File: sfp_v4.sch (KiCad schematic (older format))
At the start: 75 parts, among them J102 SMA, J104 SMA, J106 SMA, P101 SFP-CONNECTOR, P103 CONN_01X01, P106 CONN_01X01, T101 ADT2-1T, T102 ADT2-1T, U101 LMH6702, U102 LMH6702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

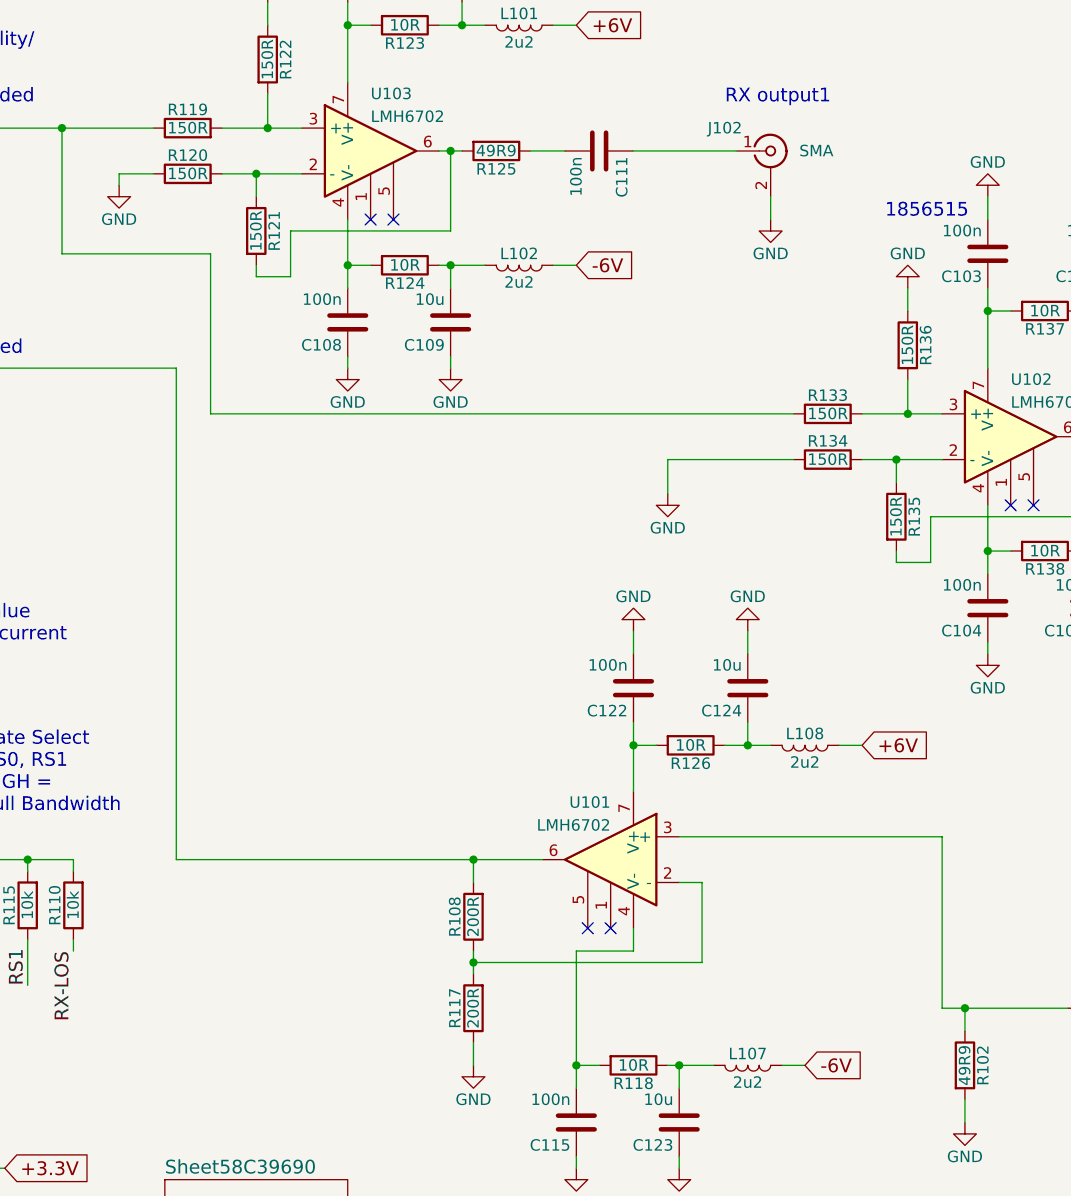
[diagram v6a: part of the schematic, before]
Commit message: bump gain to 1+240/60
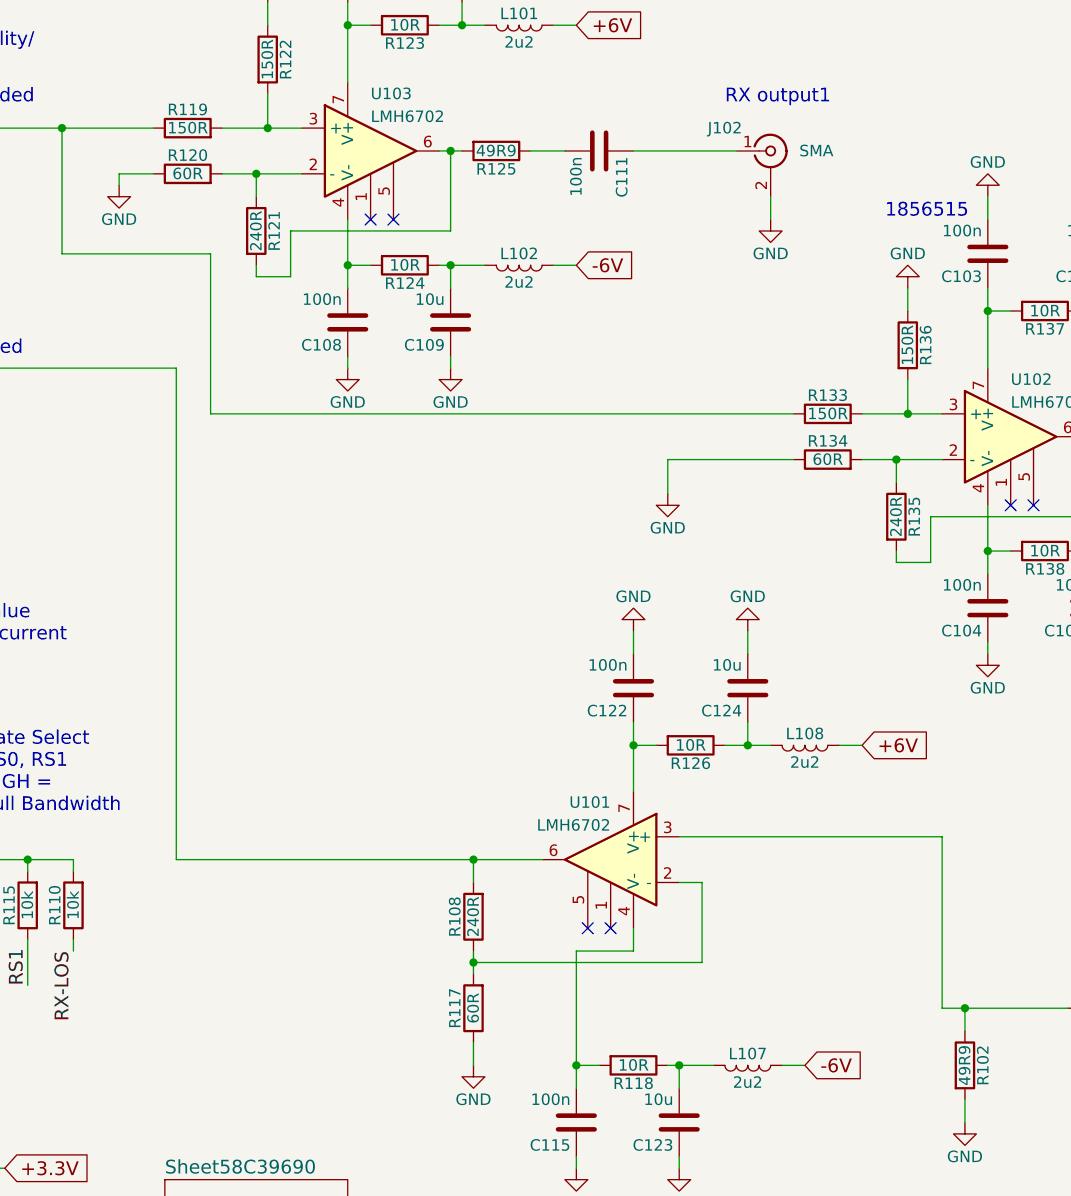
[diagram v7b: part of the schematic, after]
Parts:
- R108: value 200R -> 240R
- R117: value 200R -> 60R
- R120, R134: value 150R -> 60R
- R121, R135: value 150R -> 240R
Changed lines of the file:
@@
 P 5050 1900
 F 0 "R120" V 5130 1900 50  0000 C CNN
-F 1 "150R" V 5050 1900 50  0000 C CNN
+F 1 "60R" V 5050 1900 50  0000 C CNN
 F 2 "Resistors_SMD:R_0805" V 4980 1900 30  0001 C CNN
 F 3 "" H 5050 1900 30  0000 C CNN
@@
 P 5350 2150
 F 0 "R121" V 5430 2150 50  0000 C CNN
-F 1 "150R" V 5350 2150 50  0000 C CNN
+F 1 "240R" V 5350 2150 50  0000 C CNN
 F 2 "Resistors_SMD:R_0805" V 5280 2150 30  0001 C CNN
 F 3 "" H 5350 2150 30  0000 C CNN
@@
 P 8150 3400
 F 0 "R135" V 8230 3400 50  0000 C CNN
-F 1 "150R" V 8150 3400 50  0000 C CNN
+F 1 "240R" V 8150 3400 50  0000 C CNN
 F 2 "Resistors_SMD:R_0805" V 8080 3400 30  0001 C CNN
 F 3 "" H 8150 3400 30  0000 C CNN
@@
 P 7850 3150
 F 0 "R134" V 7930 3150 50  0000 C CNN
-F 1 "150R" V 7850 3150 50  0000 C CNN
+F 1 "60R" V 7850 3150 50  0000 C CNN
 F 2 "Resistors_SMD:R_0805" V 7780 3150 30  0001 C CNN
 F 3 "" H 7850 3150 30  0000 C CNN
@@
 P 6300 5150
 F 0 "R108" V 6380 5150 50  0000 C CNN
-F 1 "200R" V 6300 5150 50  0000 C CNN
+F 1 "240R" V 6300 5150 50  0000 C CNN
 F 2 "Resistors_SMD:R_0805" V 6230 5150 50  0001 C CNN
 F 3 "" H 6300 5150 50  0001 C CNN
@@
 P 6300 5550
 F 0 "R117" V 6380 5550 50  0000 C CNN
-F 1 "200R" V 6300 5550 50  0000 C CNN
+F 1 "60R" V 6300 5550 50  0000 C CNN
 F 2 "Resistors_SMD:R_0805" V 6230 5550 50  0001 C CNN
 F 3 "" H 6300 5550 50  0001 C CNN

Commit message: tune component values
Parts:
- R108: value 240R -> 200R
- R117: value 60R -> 200R
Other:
- note removed: "BNC: 1076295"
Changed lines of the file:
@@
 Text Notes 3250 7200 0    60   ~ 0
 1u Inductor\n445-6756-1-ND
-Text Notes 10300 5050 0    60   ~ 0
-BNC: 1076295
 $Comp
 L sfp_v4-rescue:C C114
@@
 P 6300 5150
 F 0 "R108" V 6380 5150 50  0000 C CNN
-F 1 "240R" V 6300 5150 50  0000 C CNN
+F 1 "200R" V 6300 5150 50  0000 C CNN
 F 2 "Resistors_SMD:R_0805" V 6230 5150 50  0001 C CNN
 F 3 "" H 6300 5150 50  0001 C CNN
@@
 P 6300 5550
 F 0 "R117" V 6380 5550 50  0000 C CNN
-F 1 "60R" V 6300 5550 50  0000 C CNN
+F 1 "200R" V 6300 5550 50  0000 C CNN
 F 2 "Resistors_SMD:R_0805" V 6230 5550 50  0001 C CNN
 F 3 "" H 6300 5550 50  0001 C CNN
